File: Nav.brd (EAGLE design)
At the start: 30 x 60 mm, 47 parts, among them J1 U.FL-R-SMT, SW1 THAU13-AB-R, SW2 THAU13-AB-R, SW3 TVAF06-A020B-R, SW4 TVAF06-A020B-R, U1 LSM9DS1, U2 LPS25HB, U6 OPA340N, U7 DRIVER-LV8548MC-AH(SOIC10), U8 I-02247_NJM2845

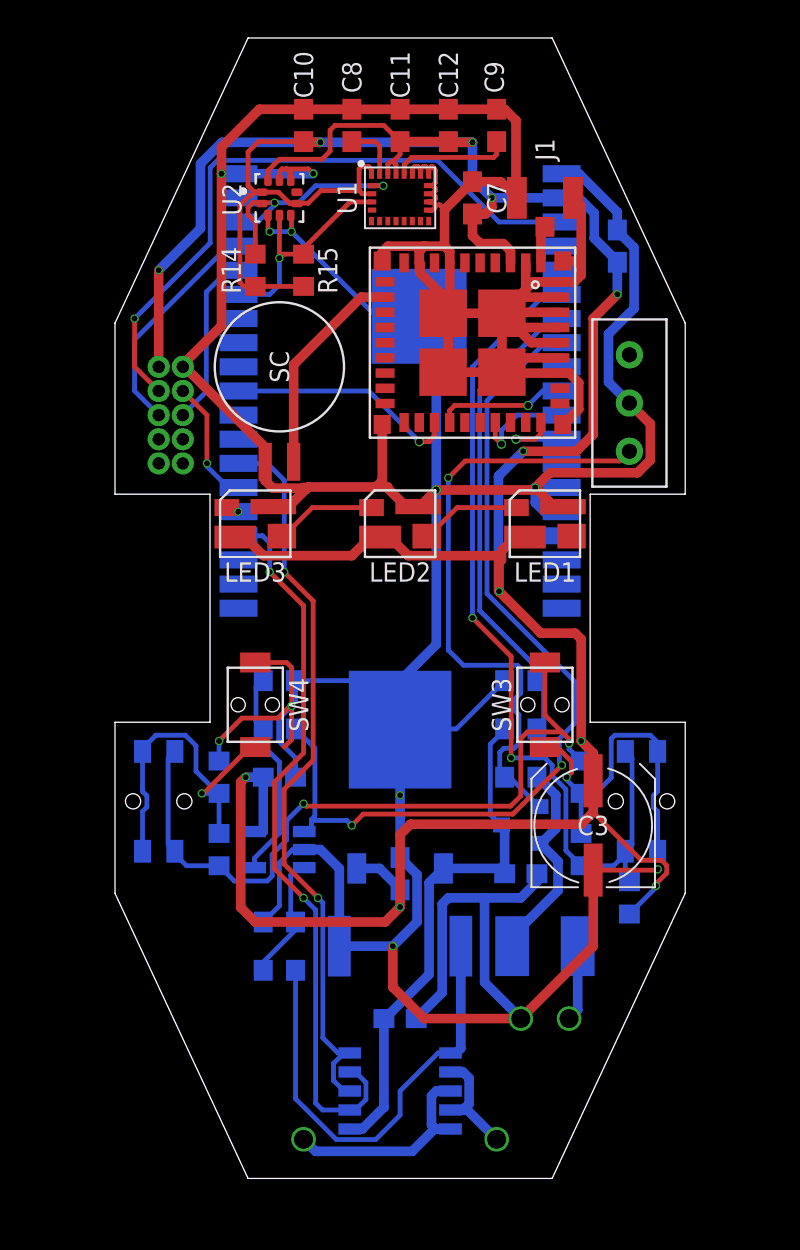
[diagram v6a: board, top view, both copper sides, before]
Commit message: Add GND plane
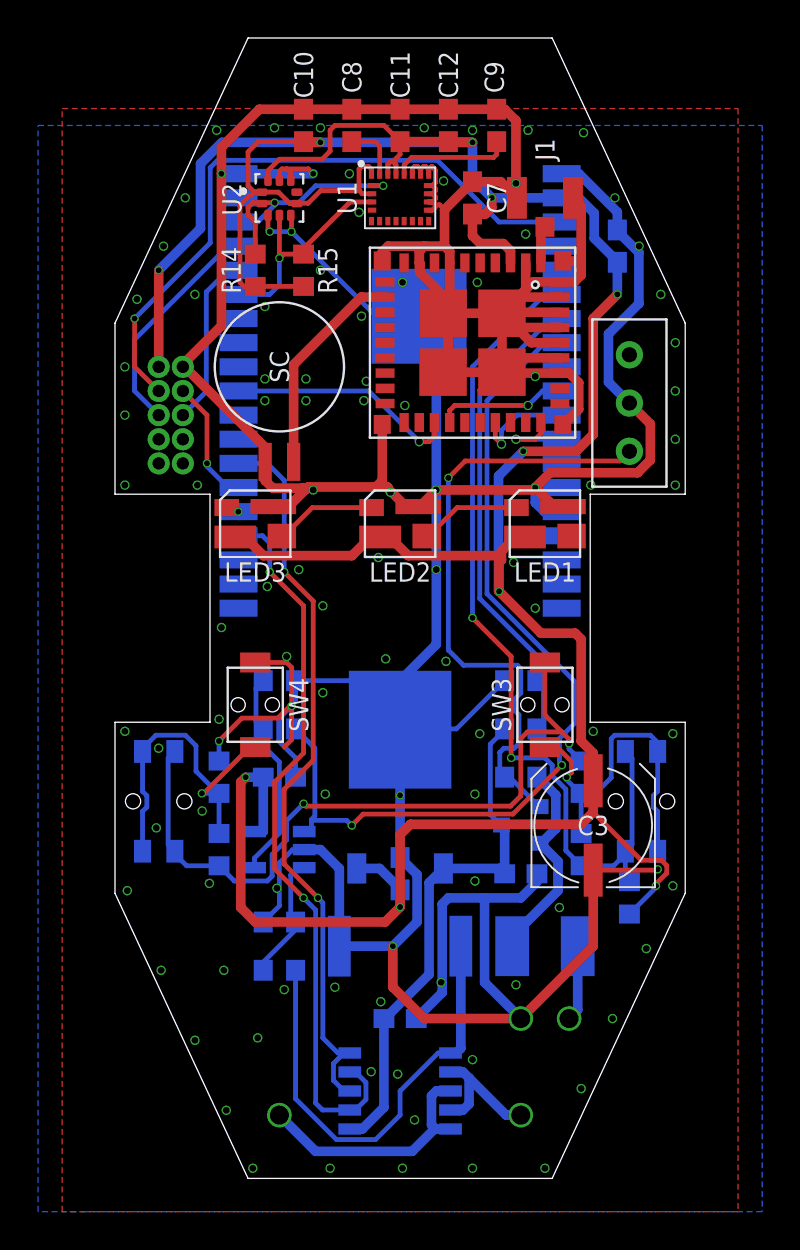
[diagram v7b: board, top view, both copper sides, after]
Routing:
- net M1: track 11.4 -> 13.2 mm
- net M2: track 5.93 -> 7.11 mm
- net GND: track 308.3 -> 308.5 mm, vias 12 -> 106
- net VDD: vias 11 -> 10
- added copper zone on layer 1, net GND
- added copper zone on layer 16, net GND
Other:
- board text added: "2022 WASA Rocket"
